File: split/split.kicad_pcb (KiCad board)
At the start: 2 copper layers, 25 parts, among them SW1 SW_Push_45deg, SW11 SW_Push_45deg, SW13 SW_Push_45deg, SW15 SW_Push_45deg, SW2 SW_Push_45deg, SW3 SW_Push_45deg, SW4 SW_Push_45deg, SW5 SW_Push_45deg, SW6 SW_Push_45deg, SW7 SW_Push_45deg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

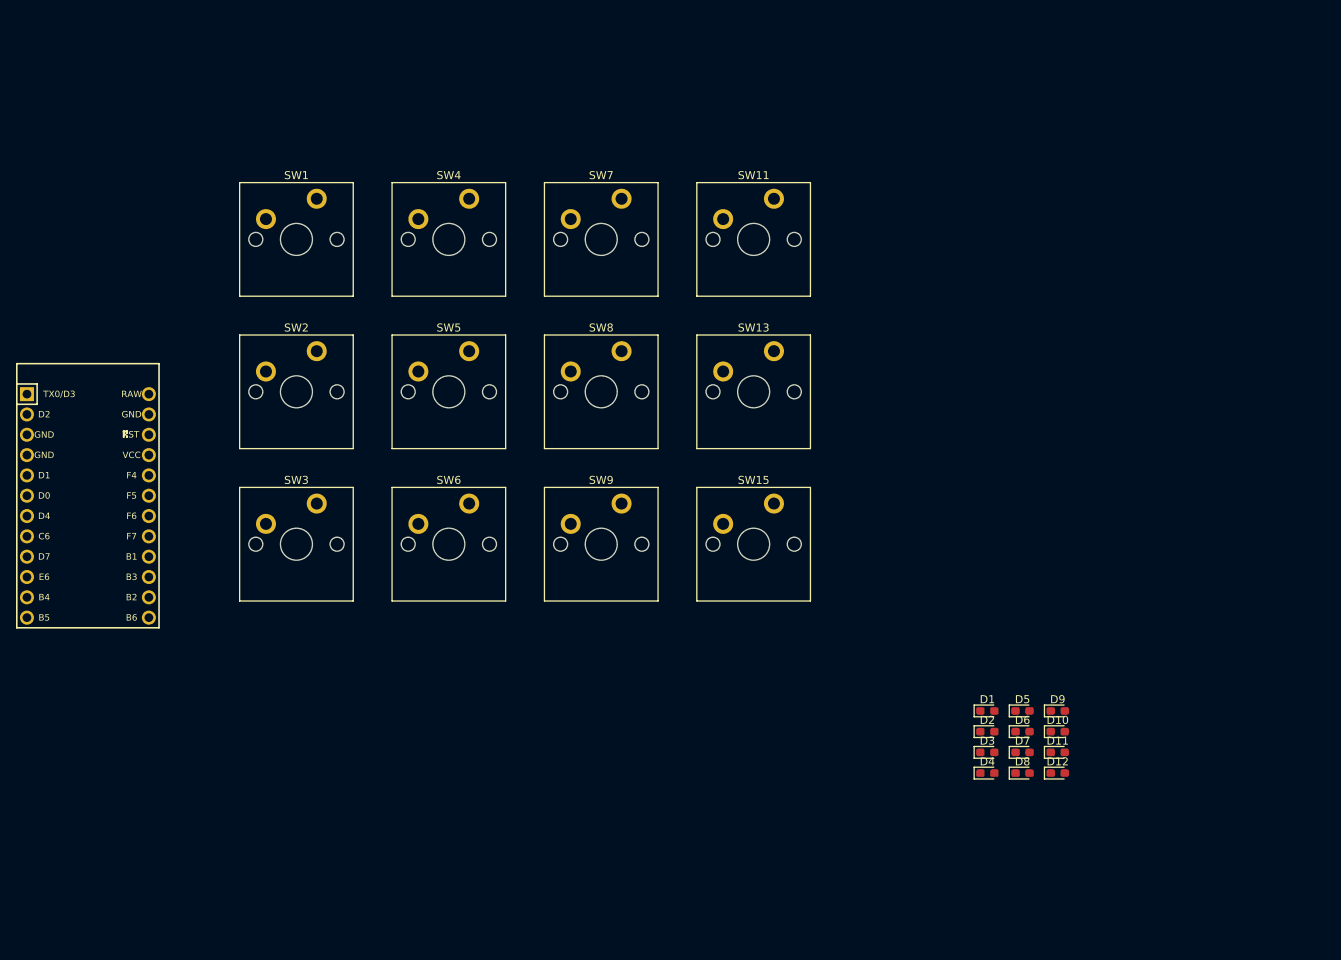
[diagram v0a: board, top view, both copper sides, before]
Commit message: start split rigth layout
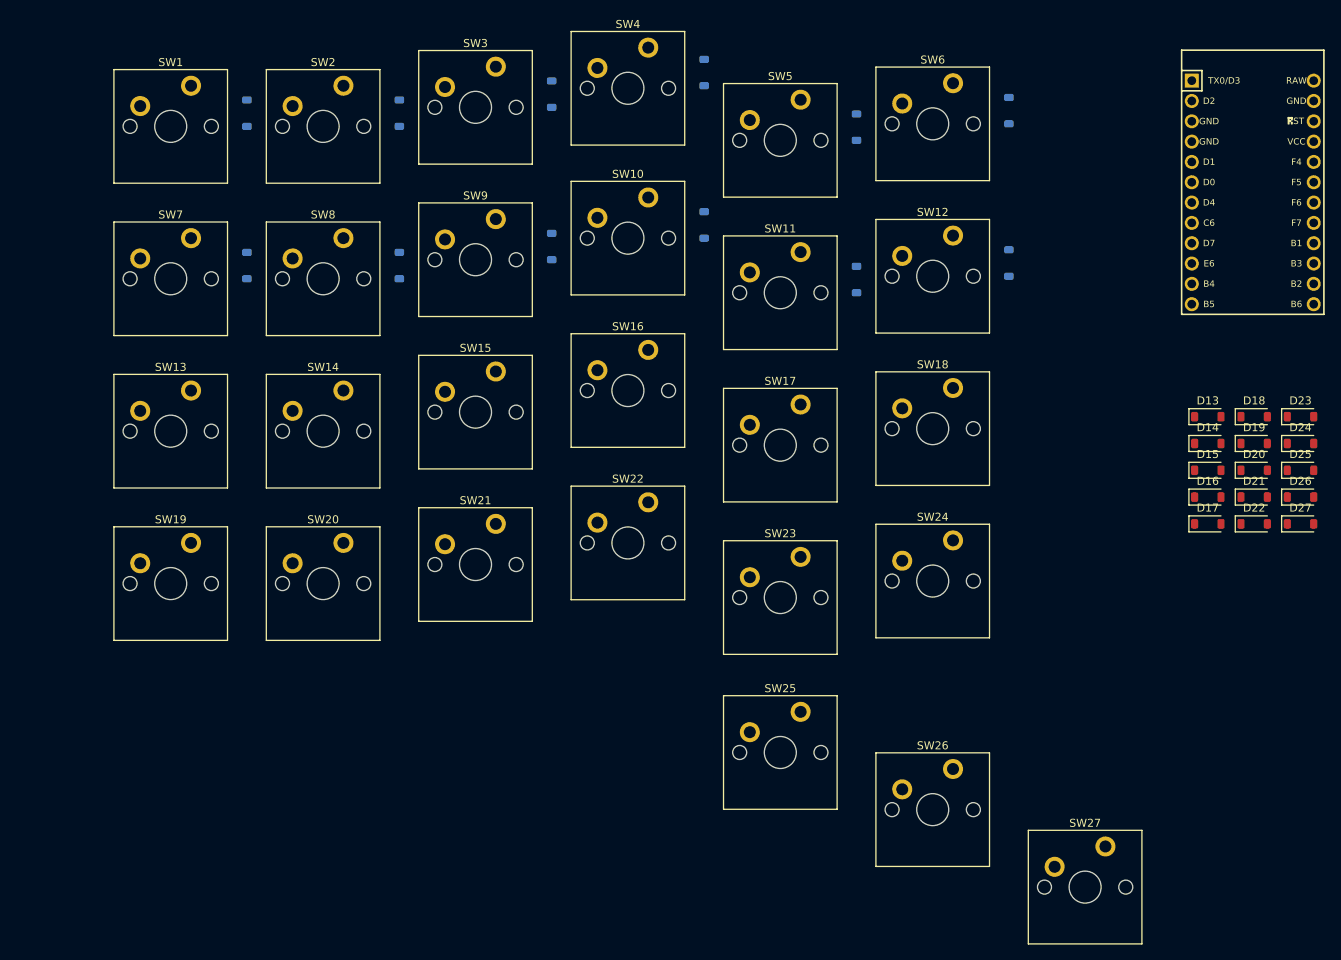
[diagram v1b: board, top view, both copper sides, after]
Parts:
- added D13: 1N4148W, Diode_SMD:D_SOD-123, F.Cu at (186.8, 81.8)
- added D14: 1N4148W, Diode_SMD:D_SOD-123, F.Cu at (186.8, 85.2)
- added D15: 1N4148W, Diode_SMD:D_SOD-123, F.Cu at (186.8, 88.5)
- added D16: 1N4148W, Diode_SMD:D_SOD-123, F.Cu at (186.8, 91.9)
- added D17: 1N4148W, Diode_SMD:D_SOD-123, F.Cu at (186.8, 95.2)
- added D18: 1N4148W, Diode_SMD:D_SOD-123, F.Cu at (192.6, 81.8)
- added D19: 1N4148W, Diode_SMD:D_SOD-123, F.Cu at (192.6, 85.2)
- added D20: 1N4148W, Diode_SMD:D_SOD-123, F.Cu at (192.6, 88.5)
- added D21: 1N4148W, Diode_SMD:D_SOD-123, F.Cu at (192.6, 91.9)
- added D22: 1N4148W, Diode_SMD:D_SOD-123, F.Cu at (192.6, 95.2)
- added D23: 1N4148W, Diode_SMD:D_SOD-123, F.Cu at (198.4, 81.8)
- added D24: 1N4148W, Diode_SMD:D_SOD-123, F.Cu at (198.4, 85.2)
- added D25: 1N4148W, Diode_SMD:D_SOD-123, F.Cu at (198.4, 88.5)
- added D26: 1N4148W, Diode_SMD:D_SOD-123, F.Cu at (198.4, 91.9)
- added D27: 1N4148W, Diode_SMD:D_SOD-123, F.Cu at (198.4, 95.2)
- added SW13: SW_Push_45deg, ScottoKeebs_MX:MX_PCB_1.00u, F.Cu at (57.1, 83.7)
- added SW14: SW_Push_45deg, ScottoKeebs_MX:MX_PCB_1.00u, F.Cu at (76.2, 83.7)
- added SW15: SW_Push_45deg, ScottoKeebs_MX:MX_PCB_1.00u, F.Cu at (95.2, 81.3)
- added SW16: SW_Push_45deg, ScottoKeebs_MX:MX_PCB_1.00u, F.Cu at (114.3, 78.6)
- added SW17: SW_Push_45deg, ScottoKeebs_MX:MX_PCB_1.00u, F.Cu at (133.3, 85.4)
- added SW18: SW_Push_45deg, ScottoKeebs_MX:MX_PCB_1.00u, F.Cu at (152.4, 83.3)
- added SW19: SW_Push_45deg, ScottoKeebs_MX:MX_PCB_1.00u, F.Cu at (57.1, 102.7)
- added SW20: SW_Push_45deg, ScottoKeebs_MX:MX_PCB_1.00u, F.Cu at (76.2, 102.7)
- added SW21: SW_Push_45deg, ScottoKeebs_MX:MX_PCB_1.00u, F.Cu at (95.2, 100.3)
- added SW22: SW_Push_45deg, ScottoKeebs_MX:MX_PCB_1.00u, F.Cu at (114.3, 97.6)
- added SW23: SW_Push_45deg, ScottoKeebs_MX:MX_PCB_1.00u, F.Cu at (133.3, 104.5)
- added SW24: SW_Push_45deg, ScottoKeebs_MX:MX_PCB_1.00u, F.Cu at (152.4, 102.4)
- added SW25: SW_Push_45deg, ScottoKeebs_MX:MX_PCB_1.00u, F.Cu at (133.3, 123.8)
- added SW26: SW_Push_45deg, ScottoKeebs_MX:MX_PCB_1.00u, F.Cu at (152.4, 131.0)
- added SW27: SW_Push_45deg, ScottoKeebs_MX:MX_PCB_1.00u, F.Cu at (171.4, 140.7)
- D1, D10, D11, D12, D2, D3, D4, D5, D6, D7, D8, D9: value 1N4148 -> 1N4148W; footprint Diode_SMD:D_0603_1608Metric_Pad1.05x0.95mm_HandSolder -> Diode_SMD:D_SOD-123; moved to B.Cu
- moved U1 150.8 mm to (192.4, 53.8)
- moved D1 119.0 mm to (66.7, 43.9), turned to 90 degrees
- moved D7 114.5 mm to (66.7, 63.0), turned to 90 degrees
- moved D2 106.7 mm to (85.7, 43.9), turned to 90 degrees
- moved D8 100.5 mm to (85.7, 63.0), turned to -90 degrees
- moved D3 98.7 mm to (104.8, 41.5), turned to 90 degrees
- moved D4 94.5 mm to (123.8, 38.8), turned to 90 degrees
- moved D9 85.9 mm to (104.8, 60.6), turned to 90 degrees
- moved SW6 80.1 mm to (152.4, 45.2)
- moved D6 77.6 mm to (161.9, 43.6), turned to 90 degrees
- moved D10 77.2 mm to (123.8, 57.9), turned to 90 degrees
- moved D5 75.9 mm to (142.9, 45.7), turned to 90 degrees
- moved D11 64.2 mm to (142.9, 64.7), turned to 90 degrees
- moved D12 64.0 mm to (161.9, 62.6), turned to 90 degrees
- moved SW3 59.0 mm to (95.2, 43.2)
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- renumbered SW11 to SW10, SW13 to SW11, SW15 to SW12
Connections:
- D10 pad 1: /ROW0 -> /ROW1
- D11 pad 1: /ROW0 -> /ROW1
- D12 pad 1: /ROW0 -> /ROW1
- D5 pad 1: /ROW1 -> /ROW0
- D6 pad 1: /ROW1 -> /ROW0
- D9 pad 1: /ROW0 -> /ROW1
- SW10 pad 1: /COL1 -> /COL3
- SW11 pad 1: /COL2 -> /COL4
- SW12 pad 1: /COL3 -> /COL5
- SW5 pad 1: /COL0 -> /COL4
- SW6 pad 1: /COL1 -> /COL5
- SW7 pad 1: /COL2 -> /COL0
- SW8 pad 1: /COL3 -> /COL1
- SW9 pad 1: /COL0 -> /COL2

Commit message: add arduino pro micro equivalent MCU schematic
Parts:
- removed U1: Arduino_Pro_Micro, ScottoKeebs_MCU:Arduino_Pro_Micro
- added C1: 22pF, Capacitor_SMD:C_0603_1608Metric_Pad1.08x0.95mm_HandSolder, B.Cu at (74.8, 61.0)
- added C2: 22pF, Capacitor_SMD:C_0603_1608Metric_Pad1.08x0.95mm_HandSolder, B.Cu at (74.8, 63.6)
- added C3: 1uF, Capacitor_SMD:C_0603_1608Metric_Pad1.08x0.95mm_HandSolder, B.Cu at (74.8, 66.1)
- added D28: LED, LED_SMD:LED_0603_1608Metric_Pad1.05x0.95mm_HandSolder, B.Cu at (70.4, 68.2)
- added D29: LED, LED_SMD:LED_0603_1608Metric_Pad1.05x0.95mm_HandSolder, B.Cu at (70.4, 70.8)
- added D30: LED, LED_SMD:LED_0603_1608Metric_Pad1.05x0.95mm_HandSolder, B.Cu at (70.4, 73.4)
- added F1: 500mA, Fuse:Fuse_0603_1608Metric_Pad1.05x0.95mm_HandSolder, B.Cu at (74.8, 68.6)
- added J1: USB_B_Micro, Connector_USB:USB_Micro-B_Molex-105017-0001, B.Cu at (67.7, 62.8)
- added R1: 1K, Fuse:Fuse_0603_1608Metric_Pad1.05x0.95mm_HandSolder, B.Cu at (74.8, 71.1)
- added R2: 1K, Resistor_SMD:R_0603_1608Metric_Pad0.98x0.95mm_HandSolder, B.Cu at (74.8, 73.6)
- added R3: 22R, Resistor_SMD:R_0603_1608Metric_Pad0.98x0.95mm_HandSolder, B.Cu at (74.8, 76.1)
- added R4: 22R, Resistor_SMD:R_0603_1608Metric_Pad0.98x0.95mm_HandSolder, B.Cu at (74.8, 78.6)
- added R5: 10K, Resistor_SMD:R_0603_1608Metric_Pad0.98x0.95mm_HandSolder, B.Cu at (74.8, 81.1)
- added R6: 1K, Resistor_SMD:R_0603_1608Metric_Pad0.98x0.95mm_HandSolder, B.Cu at (74.8, 83.6)
- added U2: ATmega32U4-M, Package_DFN_QFN:QFN-44-1EP_7x7mm_P0.5mm_EP5.2x5.2mm, B.Cu at (84.0, 71.6)
- added Y1: 16MHz, Oscillator:Oscillator_SMD_Abracon_ASE-4Pin_3.2x2.5mm_HandSoldering, B.Cu at (69.5, 77.4)
- D13, D14, D15, D16, D17, D18, D19, D20, D21, D22, D23, D24, D25, D26, D27: moved to B.Cu
- moved D23 57.9 mm to (140.7, 86.9), turned to 180 degrees
- moved D24 57.9 mm to (140.7, 90.3), turned to 180 degrees
- moved D25 57.9 mm to (140.7, 93.6), turned to 180 degrees
- moved D26 57.9 mm to (140.7, 97.0), turned to 180 degrees
- moved D27 57.9 mm to (140.7, 100.3), turned to 180 degrees
- moved D18 46.3 mm to (146.5, 86.9), turned to 180 degrees
- moved D19 46.3 mm to (146.5, 90.3), turned to 180 degrees
- moved D20 46.3 mm to (146.5, 93.6), turned to 180 degrees
- moved D21 46.3 mm to (146.5, 97.0), turned to 180 degrees
- moved D22 46.3 mm to (146.5, 100.3), turned to 180 degrees
- moved D13 34.9 mm to (152.3, 86.9), turned to 180 degrees
- moved D14 34.9 mm to (152.3, 90.3), turned to 180 degrees
- moved D15 34.9 mm to (152.3, 93.6), turned to 180 degrees
- moved D16 34.9 mm to (152.3, 97.0), turned to 180 degrees
- moved D17 34.9 mm to (152.3, 100.3), turned to 180 degrees
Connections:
- net /COL0 renamed /key-matrix/COL0
- net /COL1 renamed /key-matrix/COL1
- net /COL2 renamed /key-matrix/COL2
- net /COL3 renamed /key-matrix/COL3
- net /COL4 renamed /key-matrix/COL4
- net /COL5 renamed /key-matrix/COL5
- net /ROW0 renamed /key-matrix/ROW0
- net /ROW1 renamed /key-matrix/ROW1
- net /ROW2 renamed /key-matrix/ROW2
- net /ROW3 renamed /key-matrix/ROW3
- net /ROW4 renamed /key-matrix/ROW4
